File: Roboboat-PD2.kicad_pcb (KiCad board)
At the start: 2 copper layers, 78 x 60.7 mm, 40 parts, among them J1 14.4V, J10 Motor, J11 Motor, J12 Motor, J13 Motor, J14 Motor, J15 Motor, J16 Motor, J17 GND TP, J2 PGOOD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

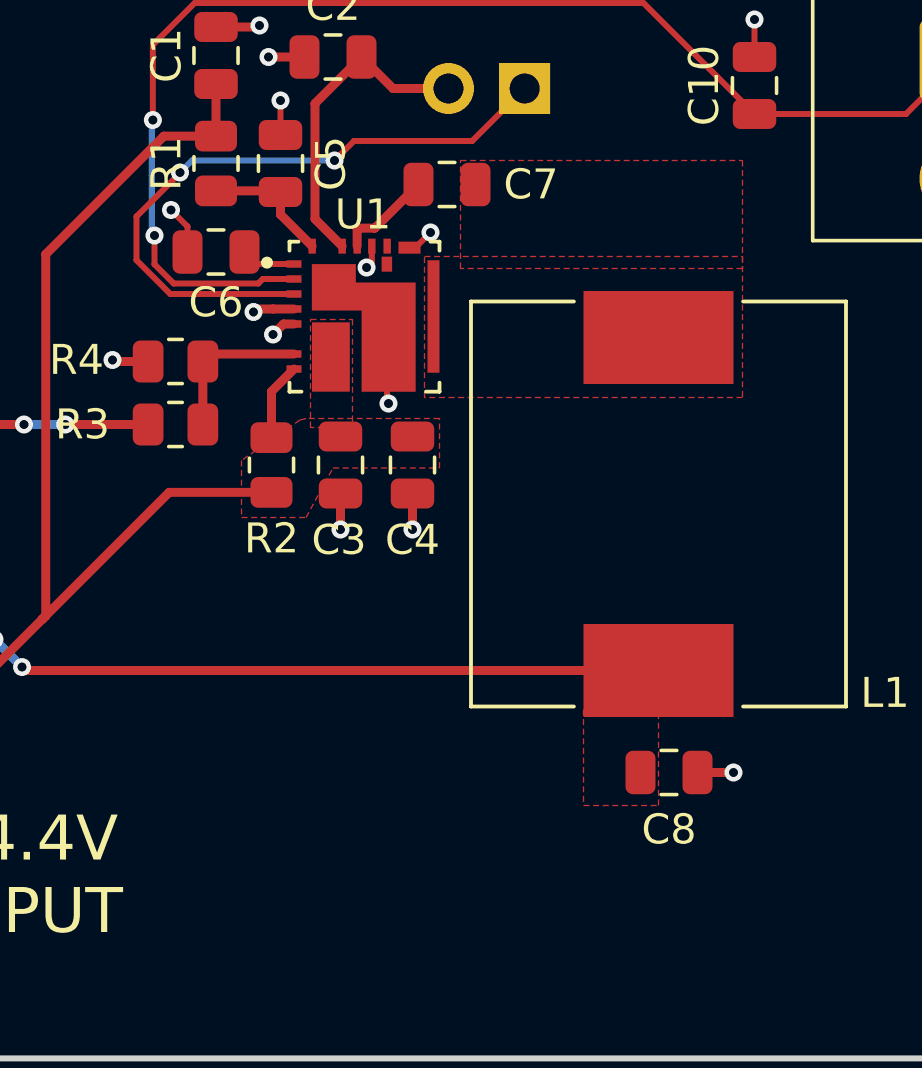
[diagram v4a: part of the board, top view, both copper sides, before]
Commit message: replace traces with fills
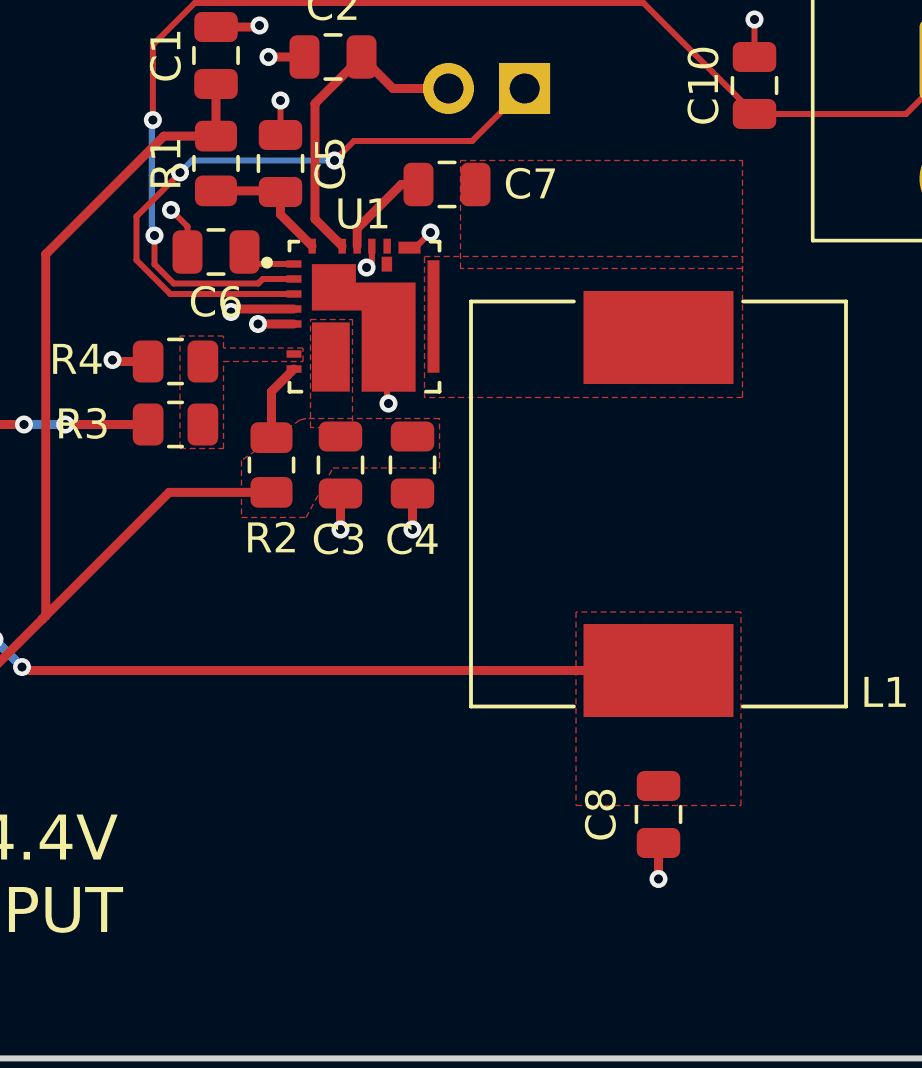
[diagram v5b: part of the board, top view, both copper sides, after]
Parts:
- moved C8 1.44 mm to (157.2, 135.2), turned to -90 degrees
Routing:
- net Net-(U1-FB): track 4.89 -> 0.00 mm
- net GND: track 21.7 -> 22.8 mm
- added copper zone on F.Cu, net Net-(U1-FB)
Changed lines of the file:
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@@
 	(footprint "Capacitor_SMD:C_0805_2012Metric"
 		(layer "F.Cu")
-		(at 157.55 133.8)
+		(at 157.2 135.2 -90)
 		(descr "Capacitor SMD 0805 (2012 Metric), square (rectangular) end terminal, IPC_7351 nominal, (Body size source: IPC-SM-782 page 76, https://www.pcb-3d.com/wordpress/wp-content/uploads/ipc-sm-782a_amendment_1_and_2.pdf, https://docs.google.com/spreadsheets/d/1BsfQQcO9C6DZCsRaXUlFlo91Tg2WpOkGARC1WS5S8t0/edit?usp=sharing), generated with kicad-footprint-generator")
 		(tags "capacitor")
 		(property "Reference" "C8"
-			(at 0 1.9 0)
+			(at 0 1.9 90)
 			(layer "F.SilkS")
 			(effects
@@
 		)
 		(property "Value" "300uF"
-			(at 0 1.68 0)
+			(at 0 1.68 90)
 			(layer "F.Fab")
 			(effects
@@
 		)
 		(property "Footprint" "Capacitor_SMD:C_0805_2012Metric"
-			(at 0 0 0)
+			(at 0 0 -90)
 			(unlocked yes)
 			(layer "F.Fab")
@@
 		)
 		(property "Datasheet" ""
-			(at 0 0 0)
+			(at 0 0 -90)
 			(unlocked yes)
 			(layer "F.Fab")
@@
 		)
 		(property "Description" "Unpolarized capacitor, small symbol"
-			(at 0 0 0)
+			(at 0 0 -90)
 			(unlocked yes)
 			(layer "F.Fab")
@@
 		(attr smd)
 		(fp_line
-			(start -0.261252 -0.735)
-			(end 0.261252 -0.735)
+			(start -0.261252 0.735)
+			(end 0.261252 0.735)
 			(stroke
 				(width 0.12)
@@
 		)
 		(fp_line
-			(start -0.261252 0.735)
-			(end 0.261252 0.735)
+			(start -0.261252 -0.735)
+			(end 0.261252 -0.735)
 			(stroke
 				(width 0.12)
@@
 		)
 		(fp_line
-			(start -1.7 -0.98)
-			(end 1.7 -0.98)
+			(start -1.7 0.98)
+			(end -1.7 -0.98)
 			(stroke
 				(width 0.05)
@@
 		)
 		(fp_line
-			(start -1.7 0.98)
-			(end -1.7 -0.98)
+			(start 1.7 0.98)
+			(end -1.7 0.98)
 			(stroke
 				(width 0.05)
@@
 		)
 		(fp_line
-			(start 1.7 -0.98)
-			(end 1.7 0.98)
+			(start -1.7 -0.98)
+			(end 1.7 -0.98)
 			(stroke
 				(width 0.05)
@@
 		)
 		(fp_line
-			(start 1.7 0.98)
-			(end -1.7 0.98)
+			(start 1.7 -0.98)
+			(end 1.7 0.98)
 			(stroke
 				(width 0.05)
@@
 		)
 		(fp_line
-			(start -1 -0.625)
-			(end 1 -0.625)
+			(start -1 0.625)
+			(end -1 -0.625)
 			(stroke
 				(width 0.1)
@@
 		)
 		(fp_line
-			(start -1 0.625)
-			(end -1 -0.625)
+			(start 1 0.625)
+			(end -1 0.625)
 			(stroke
 				(width 0.1)
@@
 		)
 		(fp_line
-			(start 1 -0.625)
-			(end 1 0.625)
+			(start -1 -0.625)
+			(end 1 -0.625)
 			(stroke
 				(width 0.1)
@@
 		)
 		(fp_line
-			(start 1 0.625)
-			(end -1 0.625)
+			(start 1 -0.625)
+			(end 1 0.625)
 			(stroke
 				(width 0.1)
@@
 		)
 		(fp_text user "${REFERENCE}"
-			(at 0 0 0)
+			(at 0 0 90)
 			(layer "F.Fab")
 			(effects
@@
 		)
 		(pad "1" smd roundrect
-			(at -0.95 0)
+			(at -0.95 0 270)
 			(size 1 1.45)
 			(layers "F.Cu" "F.Paste" "F.Mask")
@@
 		)
 		(pad "2" smd roundrect
-			(at 0.95 0)
+			(at 0.95 0 270)
 			(size 1 1.45)
 			(layers "F.Cu" "F.Paste" "F.Mask")
@@
 	)
 	(segment
-		(start 145.05 118.85)
-		(end 144.7 118.85)
-		(width 0.3)
+		(start 148.15 119.255)
+		(end 148.15 121.45)
+		(width 0.2)
 		(layer "F.Cu")
 		(net 1)
 	)
 	(segment
-		(start 148.15 119.255)
-		(end 148.15 121.45)
-		(width 0.2)
+		(start 145.05 118.85)
+		(end 143.85 118.85)
+		(width 0.3)
 		(layer "F.Cu")
 		(net 1)
@@
 	)
 	(segment
-		(start 143.8 118.35)
-		(end 143.7 118.45)
-		(width 0.3)
-		(layer "F.Cu")
-		(net 1)
-	)
-	(segment
 		(start 148.15 121.45)
 		(end 148.2 121.5)
@@
 	)
 	(segment
-		(start 144.35 118.35)
-		(end 143.8 118.35)
-		(width 0.3)
-		(layer "F.Cu")
-		(net 1)
-	)
-	(segment
 		(start 141.5 115.6)
 		(end 140.95 115.05)
@@
 	)
 	(segment
-		(start 145.05 118.35)
-		(end 144.35 118.35)
-		(width 0.3)
-		(layer "F.Cu")
-		(net 1)
-	)
-	(segment
 		(start 144.6 112.55)
 		(end 144.6 111.4)
@@
 	)
 	(segment
+		(start 143.05 118.35)
+		(end 142.95 118.45)
+		(width 0.3)
+		(layer "F.Cu")
+		(net 1)
+	)
+	(segment
 		(start 141.5 116.45)
 		(end 141.5 115.6)
@@
 	)
 	(segment
-		(start 158.5 133.8)
-		(end 159.7 133.8)
+		(start 157.2 136.15)
+		(end 157.2 137.35)
 		(width 0.3)
 		(layer "F.Cu")
@@
 	)
 	(segment
-		(start 144.7 118.85)
-		(end 144.35 119.2)
+		(start 145.05 118.35)
+		(end 143.05 118.35)
 		(width 0.3)
 		(layer "F.Cu")
@@
 	)
 	(via
-		(at 159.7 133.8)
+		(at 157.2 137.35)
 		(size 0.6)
 		(drill 0.3)
@@
 	)
 	(via
-		(at 143.7 118.45)
+		(at 143.9 108.9)
 		(size 0.6)
 		(drill 0.3)
@@
 	)
 	(via
-		(at 143.9 108.9)
+		(at 149 125.7)
 		(size 0.6)
 		(drill 0.3)
@@
 	)
 	(via
-		(at 149 125.7)
+		(at 142.95 118.45)
 		(size 0.6)
 		(drill 0.3)
@@
 	)
 	(via
-		(at 144.35 119.2)
+		(at 148.2 121.5)
 		(size 0.6)
 		(drill 0.3)
@@
 	)
 	(via
-		(at 148.2 121.5)
+		(at 146.6 125.7)
 		(size 0.6)
 		(drill 0.3)
@@
 	)
 	(via
-		(at 146.6 125.7)
+		(at 144.2 109.95)
 		(size 0.6)
 		(drill 0.3)
@@
 	)
 	(via
-		(at 144.2 109.95)
+		(at 143.85 118.85)
 		(size 0.6)
 		(drill 0.3)
@@
 	)
 	(segment
-		(start 142.0125 120.1)
-		(end 142.0125 122.2)
-		(width 0.3)
-		(layer "F.Cu")
-		(net 4)
-	)
-	(segment
-		(start 145.05 119.85)
-		(end 142.2625 119.85)
-		(width 0.3)
-		(layer "F.Cu")
-		(net 4)
-	)
-	(segment
-		(start 147.155 115.67)
-		(end 147.155 116.255)
-		(width 0.3)
-		(layer "F.Cu")
-		(net 6)
-	)
-	(segment
-		(start 149.2 114.2)
-		(end 147.745 115.655)
+		(start 148.625 114.2)
+		(end 149.2 114.2)
 		(width 0.3)
 		(layer "F.Cu")
@@
 	)
 	(segment
-		(start 147.17 115.655)
+		(start 147.155 116.255)
 		(end 147.155 115.67)
 		(width 0.3)
@@
 	)
 	(segment
-		(start 147.745 115.655)
-		(end 147.17 115.655)
+		(start 147.155 115.67)
+		(end 148.625 114.2)
 		(width 0.3)
 		(layer "F.Cu")
@@
 		(polygon
 			(pts
-				(xy 157.2 134.9) (xy 157.2 131.7) (xy 154.7 131.7) (xy 154.7 134.9)
+				(xy 159.95 134.9) (xy 159.95 128.45) (xy 154.45 128.45) (xy 154.45 134.9)
+			)
+		)
+	)
+	(zone
+		(net 4)
+		(net_name "Net-(U1-FB)")
+		(layer "F.Cu")
+		(hatch edge 0.5)
+		(priority 2)
+		(connect_pads yes
+			(clearance 0.25)
+		)
+		(min_thickness 0.25)
+		(filled_areas_thickness no)
+		(fill yes
+			(thermal_gap 0.5)
+			(thermal_bridge_width 0.5)
+		)
+		(polygon
+			(pts
+				(xy 145.35 119.65) (xy 142.7 119.65) (xy 142.7 119.25) (xy 141.25 119.25) (xy 141.25 123) (xy 142.7 123)
+				(xy 142.7 120.1) (xy 145.35 120.1)
 			)
 		)

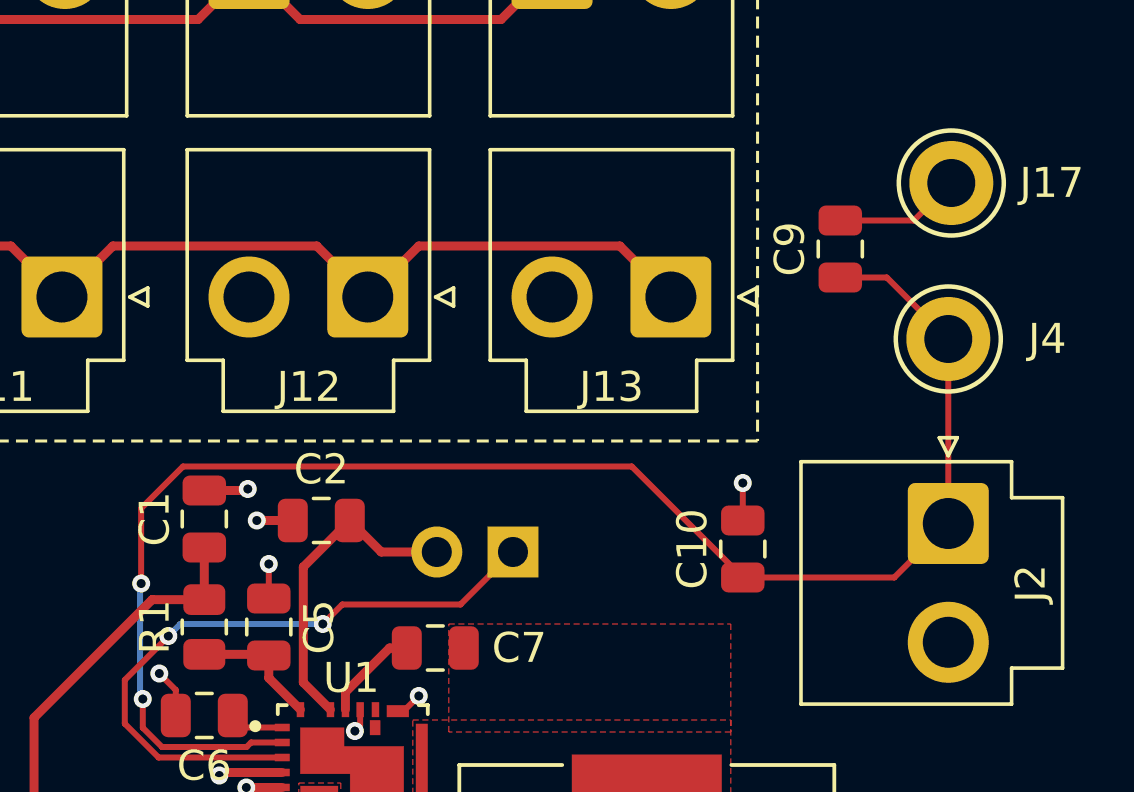
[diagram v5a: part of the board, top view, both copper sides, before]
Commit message: add pullup resistor to PGOOD
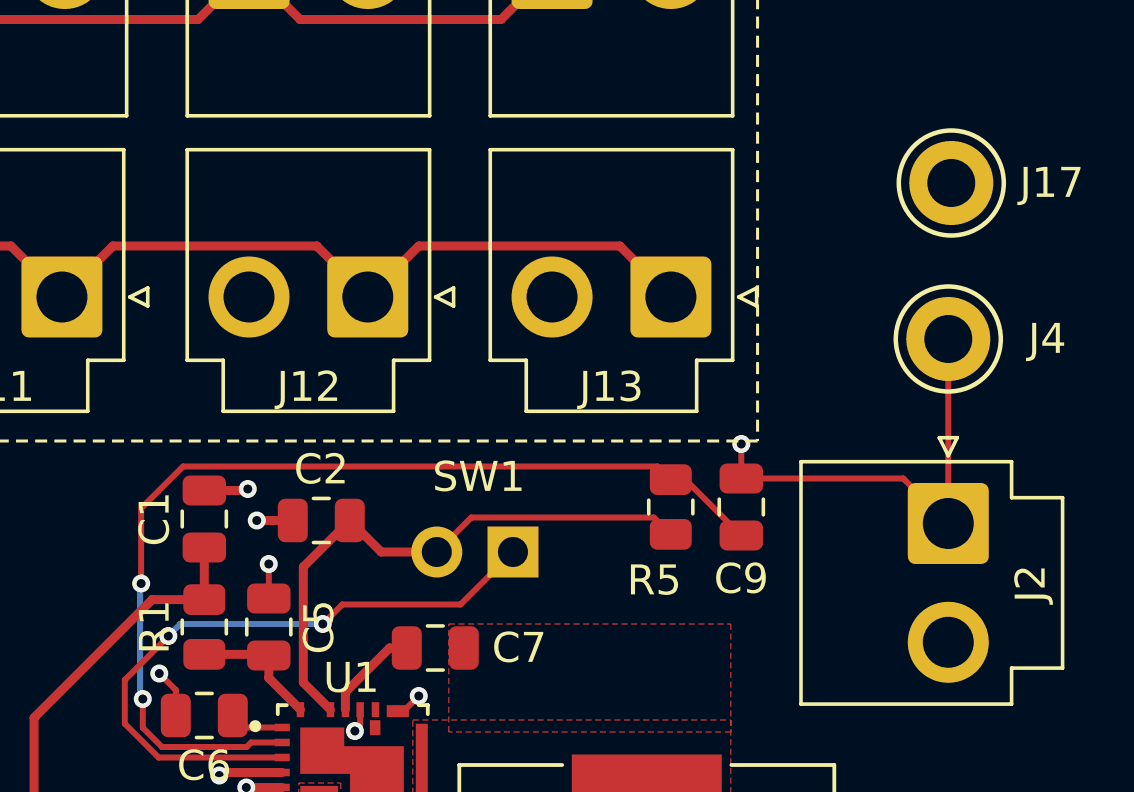
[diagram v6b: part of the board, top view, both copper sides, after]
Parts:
- removed C10: 0.1uF, Capacitor_SMD:C_0805_2012Metric
- added R5: 100k, Resistor_SMD:R_0805_2012Metric, F.Cu at (158.0, 109.5)
- moved C9 9.21 mm to (160.3, 109.5)
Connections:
- net Net-(SW1-B) renamed /VCC
- C9 pad 1: /PGOOD -> Net-(U1-PGOOD)
- C9 pad 2: GND -> /PGOOD
- U1 pad 2: /PGOOD -> Net-(U1-PGOOD)
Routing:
- net /PGOOD: track 52.7 -> 15.4 mm, vias 2 -> 1
- net Net-(U1-PGOOD): track 0.00 -> 33.9 mm, vias 0 -> 2
- net /VCC: track 10.7 -> 19.2 mm
- net GND: track 22.8 -> 17.4 mm, vias 14 -> 13
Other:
- board text added: "SW1"

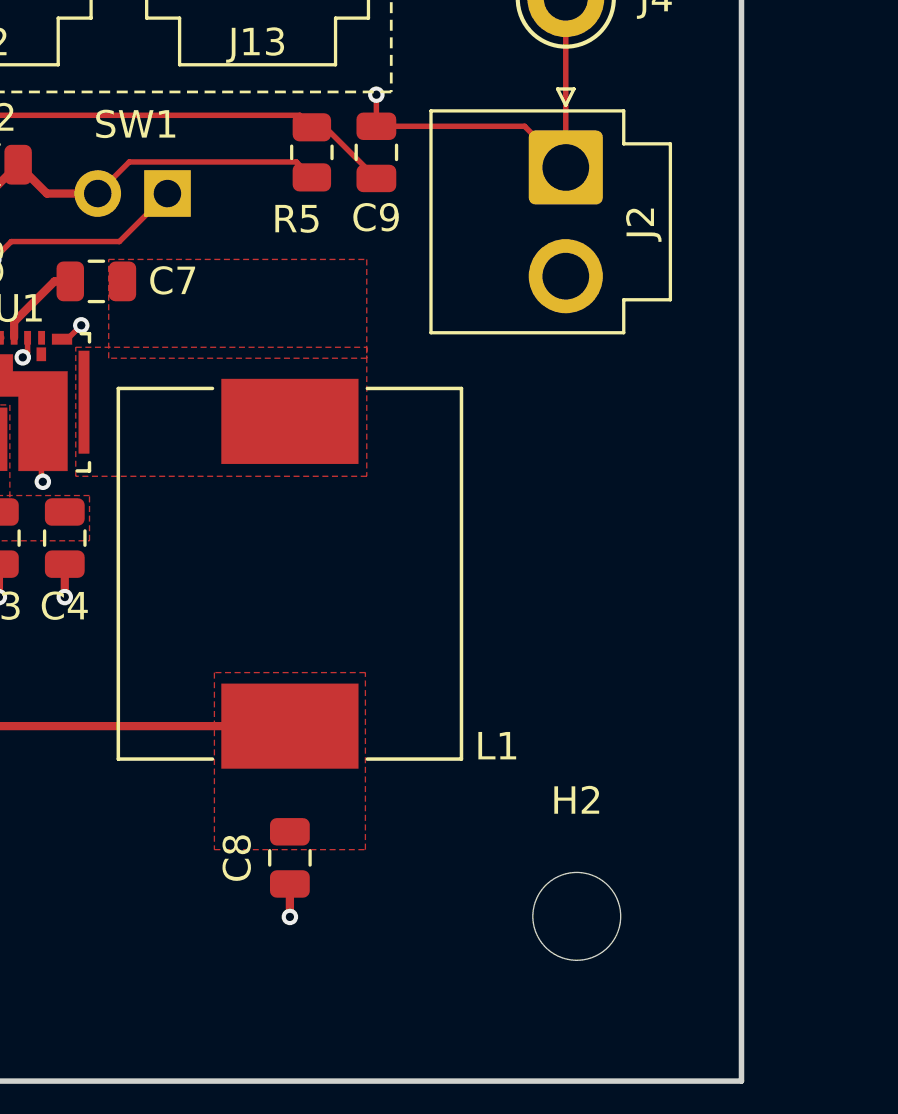
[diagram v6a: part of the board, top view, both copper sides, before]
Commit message: add status LEDs
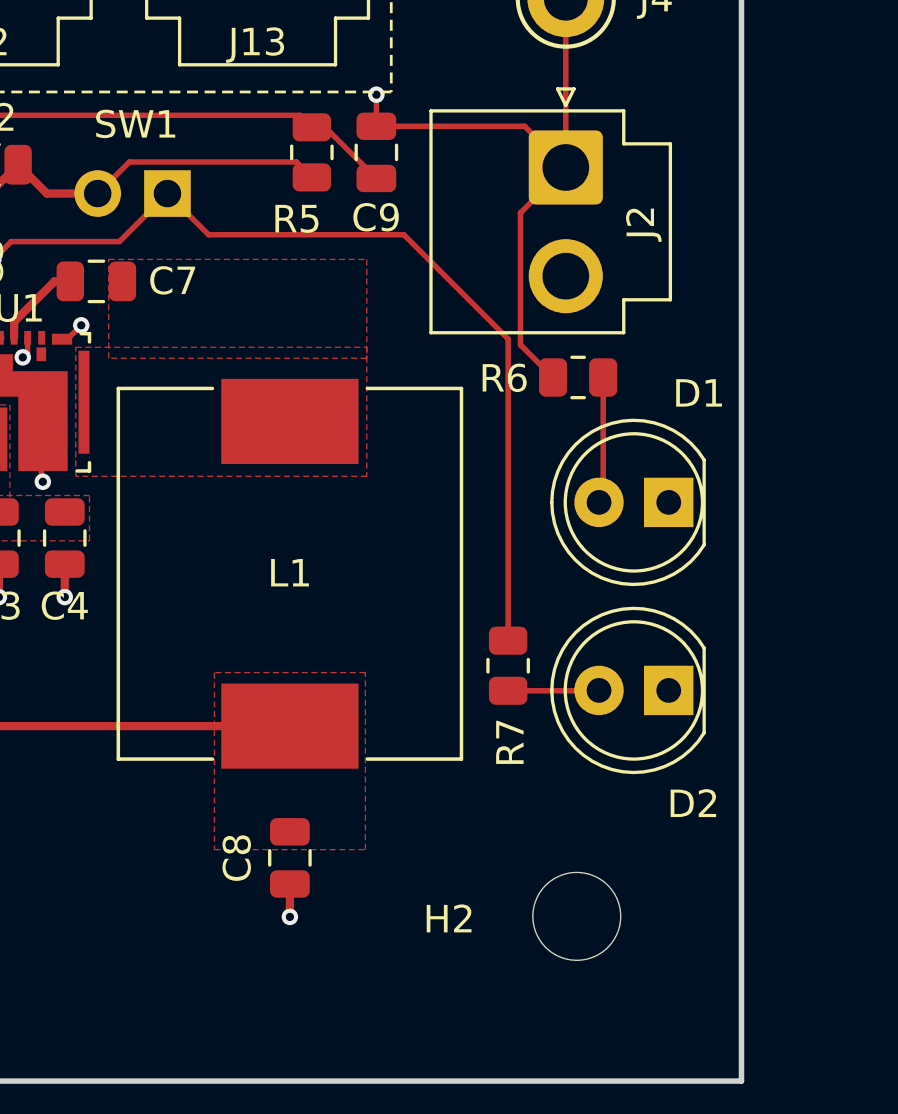
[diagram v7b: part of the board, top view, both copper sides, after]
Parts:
- added D1: GREEN LED, LED_THT:LED_D5.0mm, F.Cu at (171.0, 122.2)
- added D2: BLUE LED, LED_THT:LED_D5.0mm, F.Cu at (171.0, 129.1)
- added R6: 180, Resistor_SMD:R_0805_2012Metric, F.Cu at (167.7, 117.7)
- added R7: 180, Resistor_SMD:R_0805_2012Metric, F.Cu at (165.2, 128.2)
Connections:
- net Net-(SW1-A) renamed /EN
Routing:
- net /EN: track 21.9 -> 47.5 mm
- net /PGOOD: track 15.4 -> 23.6 mm
- net Net-(D1-A): track 0.00 -> 4.61 mm
- net Net-(D2-A): track 0.00 -> 3.32 mm
